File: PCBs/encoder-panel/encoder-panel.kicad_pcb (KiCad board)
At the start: 2 copper layers, 62.2 x 55.9 mm, 42 parts, among them J1 Conn_01x05, U1 EN1AJ-B28

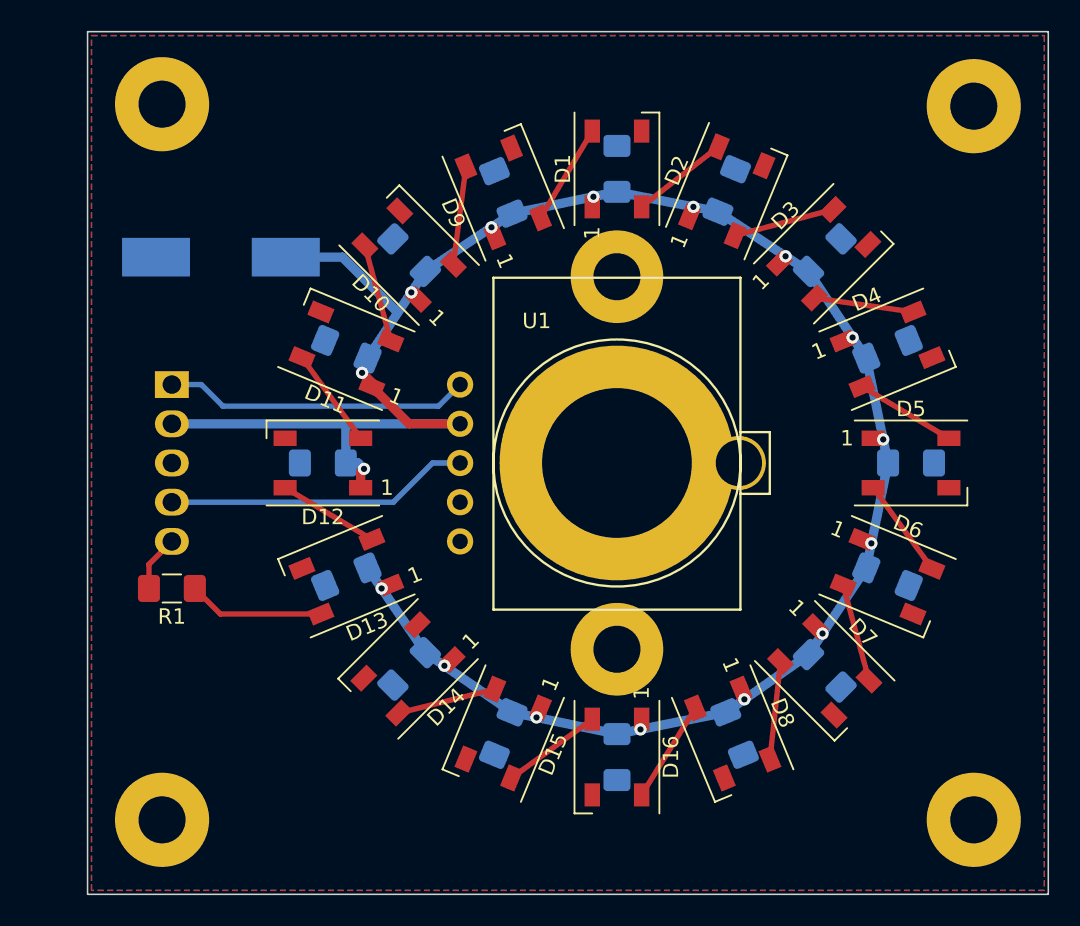
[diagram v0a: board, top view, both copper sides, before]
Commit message: Updating encoder panel PCBs (#9)
* updating encoder panel

* misc fixes

* adding oshpark page break

* renaming symbol to correct name

* removing old libraries

* tidying up footprints

* finishing

* adding images
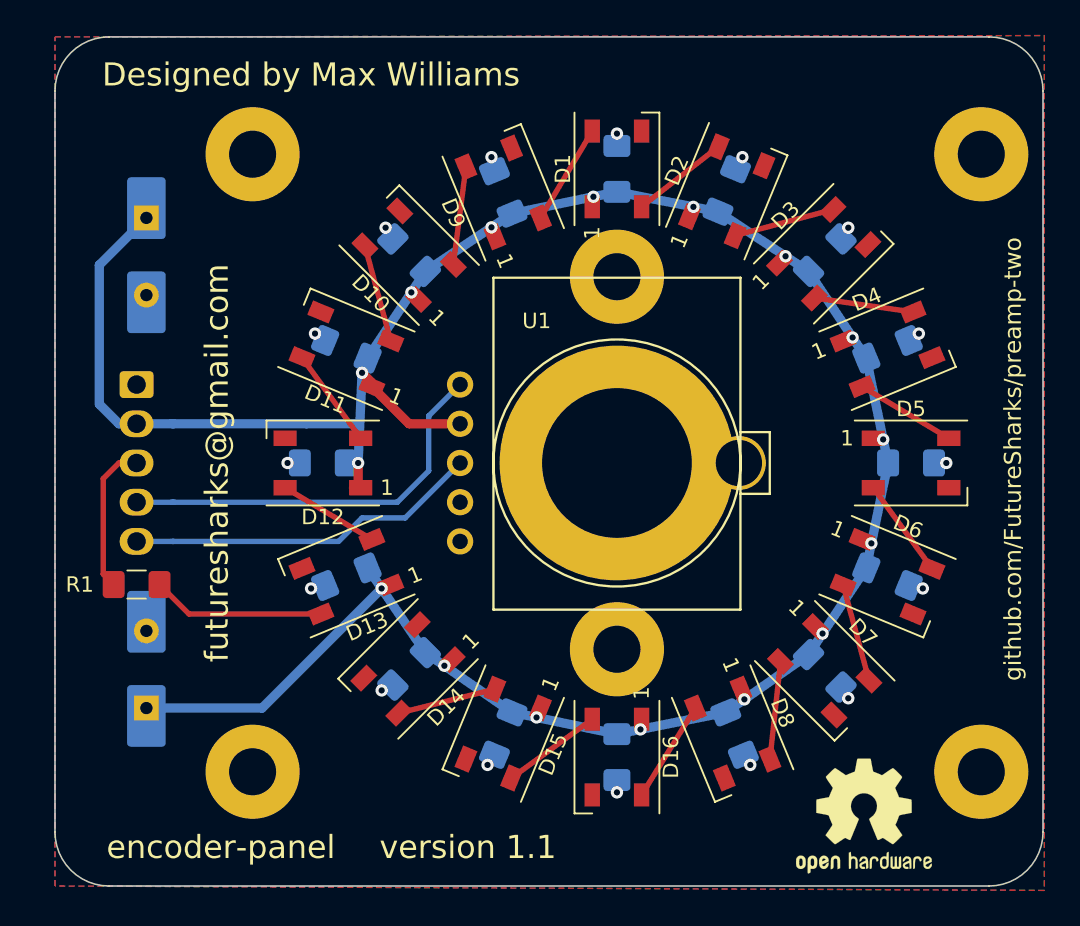
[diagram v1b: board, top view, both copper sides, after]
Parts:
- added C18: 1000uF, Capacitor_SMD:CP_Elec_8x5.4, B.Cu at (121.9, 114.9)
- added C19: 1000uF, Capacitor_THT:CP_Radial_D8.0mm_P5.00mm, B.Cu at (121.9, 85.7)
- added C20: 1000uF, Capacitor_THT:CP_Radial_D8.0mm_P5.00mm, B.Cu at (121.9, 117.5)
- added LOGO1: Logo_Open_Hardware_Small, Symbol:OSHW-Logo2_9.8x8mm_SilkScreen, B.Cu at (137.2, 124.2)
- added LOGO2: Logo_Open_Hardware_Small, Symbol:OSHW-Logo2_9.8x8mm_SilkScreen, F.Cu at (168.4, 124.5)
- C17: footprint Capacitor_SMD:CP_Elec_10x10.5 -> Capacitor_SMD:CP_Elec_8x5.4
- U1: value EN1AJ-B28 -> ENA1J-B28; footprint Bournes-EN:EN1AJ-B28-L100128L-H -> encoder-panel:ENA1J-B28-L00128L
- moved MH3 6.70 mm to (128.8, 81.6)
- moved MH5 6.64 mm to (128.8, 121.6)
- moved C17 4.83 mm to (121.9, 88.1), turned to 270 degrees
- moved MH6 3.15 mm to (176.0, 121.6)
- moved MH4 3.15 mm to (176.0, 81.6)
- moved R1 2.30 mm to (121.3, 109.5)
- moved J1 2.29 mm to (121.3, 96.5)
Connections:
- J1 pad 1: Net-(J1-Pad1) -> GND
- J1 pad 3: GND -> Net-(J1-Pad3)
- R1 pad 2: Net-(J1-Pad5) -> Net-(J1-Pad3)
- U1 pad 1: Net-(J1-Pad1) -> Net-(J1-Pad4)
- U1 pad 3: Net-(J1-Pad4) -> Net-(J1-Pad5)
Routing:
- net +5V: track 137.6 -> 162.6 mm
- net Net-(J1-Pad1): track 19.8 -> 0.00 mm
- net Net-(J1-Pad5): track 3.66 -> 23.2 mm
- net Net-(J1-Pad3): track 0.00 -> 9.72 mm
- net Net-(J1-Pad4): track 19.7 -> 26.3 mm
- net Net-(D13-Pad4): track 8.85 -> 11.2 mm
- net GND: vias 0 -> 16
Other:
- board size 62.2 x 55.9 mm -> 64 x 55 mm
- rule pad_to_mask_clearance: 0.2 -> 0.0508
- board text added: "NPxl"
- board text added: "github.com/FutureSharks/preamp-two"
- board text added: "version 1.1"
- board text removed: "NeoPxl"
- board text removed: "version 1.0"
